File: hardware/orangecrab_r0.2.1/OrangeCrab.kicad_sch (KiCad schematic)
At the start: 10 parts

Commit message: all IO gone/cleaned
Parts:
- removed FID1, FID2, FID3, FID4, FID5, FID6: Fiducial, Fiducial:Fiducial_0.75mm_Mask1.5mm, symbol Mechanical:Fiducial
- removed H1, H2: MountingHole, MountingHole:MountingHole_2.2mm_M2_Pad, symbol Mechanical:MountingHole
- removed H3, H4: MountingHole, MountingHole:MountingHole_2.1mm, symbol Mechanical:MountingHole

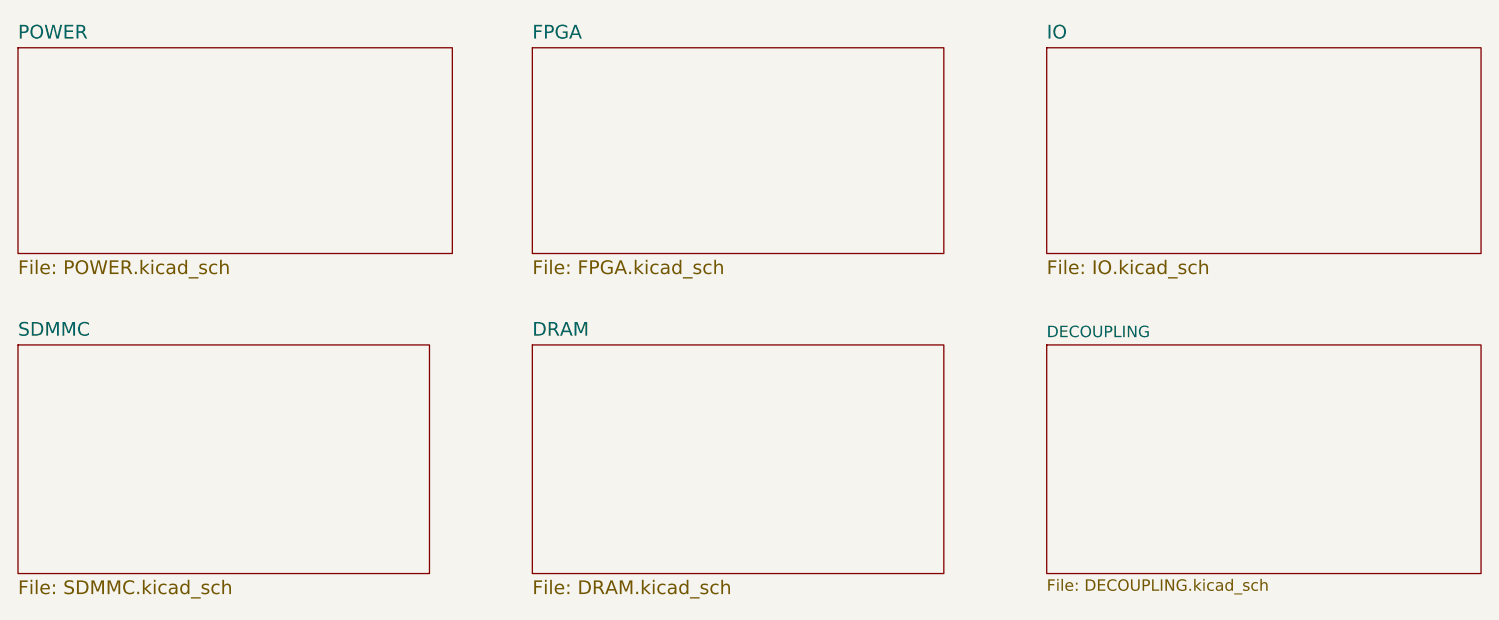
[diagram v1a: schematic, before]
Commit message: delete redundant sheets
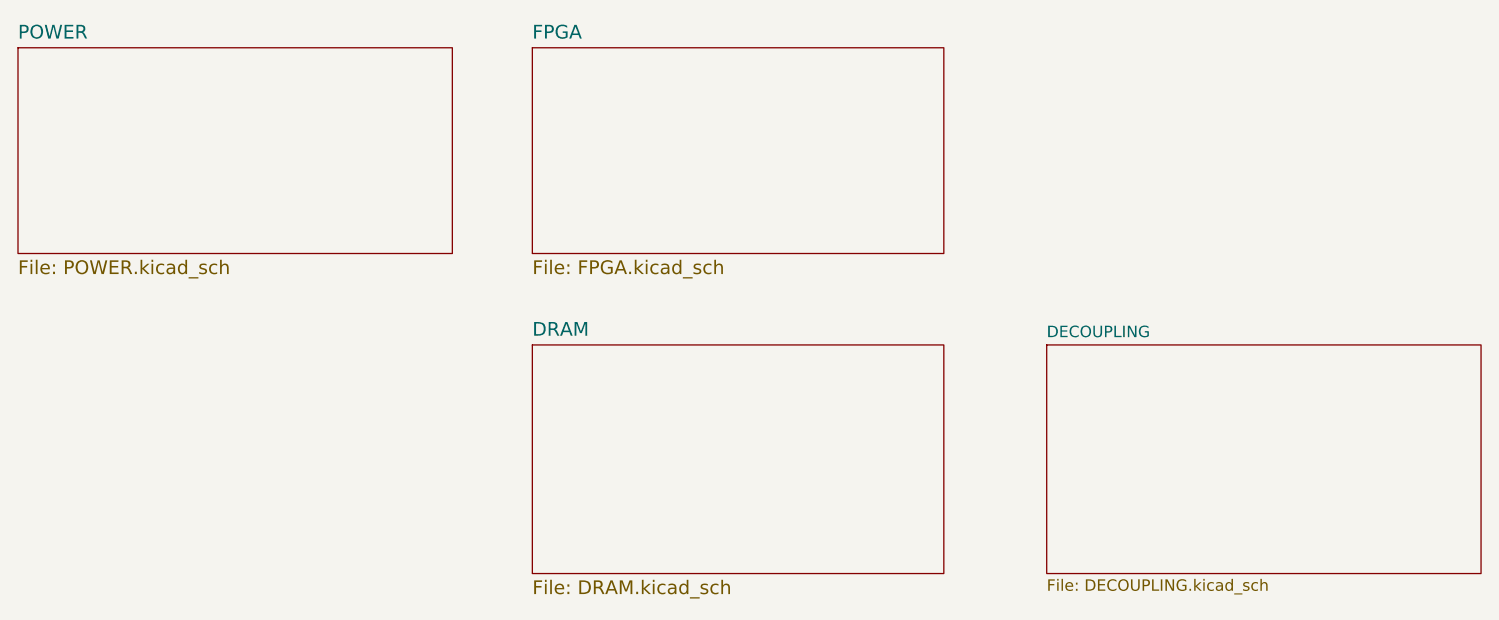
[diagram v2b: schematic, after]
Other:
- removed sheet IO
- removed sheet SDMMC
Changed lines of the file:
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@@
-    )
-  )
-  (sheet (at 160.02 73.66) (size 48.26 22.86) (fields_autoplaced)
-    (stroke (width 0) (type solid))
-    (fill (color 0 0 0 0.0000))
-    (property "Sheetname" "IO" (at 160.02 72.8214 0)
-      (effects (font (size 1.524 1.524)) (justify left bottom))
-    )
-    (property "Sheetfile" "IO.kicad_sch" (at 160.02 97.2062 0)
-      (effects (font (size 1.524 1.524)) (justify left top))
-    )
-    (instances
-      (project "OrangeCrab"
-        (path "/3fc0bb0e-dabc-4b81-bef6-ad7dd3f01477" (page "6"))
-      )
     )
   )
@@
       )
     )
-  )
-  (sheet (at 45.72 106.68) (size 45.72 25.4) (fields_autoplaced)
-    (stroke (width 0) (type solid))
-    (fill (color 0 0 0 0.0000))
-    (property "Sheetname" "SDMMC" (at 45.72 105.8414 0)
-      (effects (font (size 1.524 1.524)) (justify left bottom))
-    )
-    (property "Sheetfile" "SDMMC.kicad_sch" (at 45.72 132.7662 0)
-      (effects (font (size 1.524 1.524)) (justify left top))
-    )
-    (instances
-      (project "OrangeCrab"
-        (path "/3fc0bb0e-dabc-4b81-bef6-ad7dd3f01477" (page "3"))
-      )
-    )

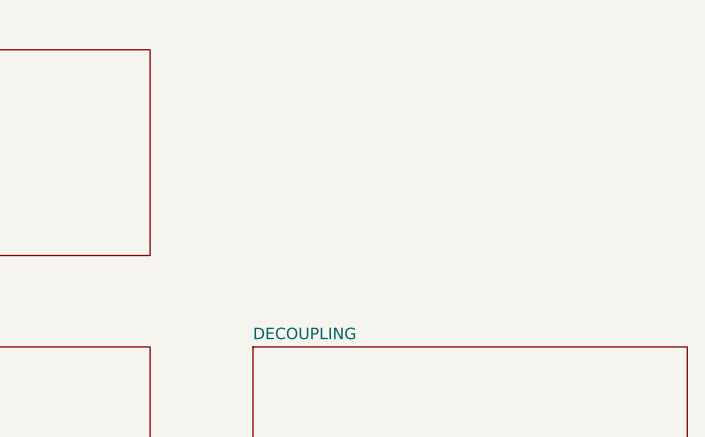
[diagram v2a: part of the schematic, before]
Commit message: M.2 form factor
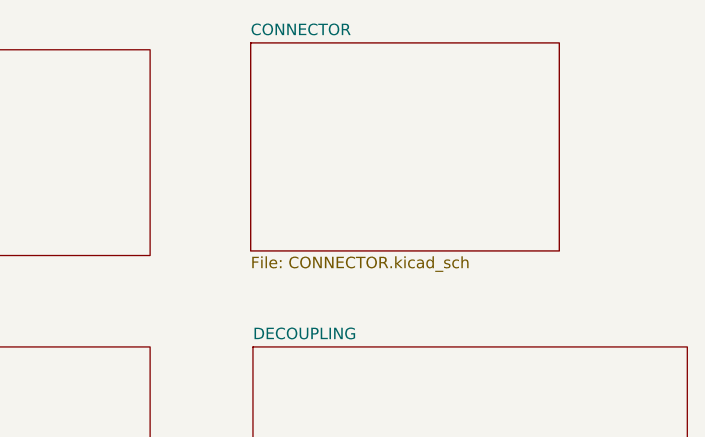
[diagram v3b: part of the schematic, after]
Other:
- added sheet CONNECTOR (CONNECTOR.kicad_sch)
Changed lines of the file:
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@@
+    )
+  )
+  (sheet (at 159.766 72.898) (size 34.29 23.114) (fields_autoplaced)
+    (stroke (width 0.1524) (type solid))
+    (fill (color 0 0 0 0.0000))
+    (property "Sheetname" "CONNECTOR" (at 159.766 72.1864 0)
+      (effects (font (size 1.27 1.27)) (justify left bottom))
+    )
+    (property "Sheetfile" "CONNECTOR.kicad_sch" (at 159.766 96.5966 0)
+      (effects (font (size 1.27 1.27)) (justify left top))
+    )
+    (instances
+      (project "OrangeCrab"
+        (path "/3fc0bb0e-dabc-4b81-bef6-ad7dd3f01477" (page "6"))
+      )
     )
   )
